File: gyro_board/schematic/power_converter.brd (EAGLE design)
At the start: 64 x 26 mm, 39 parts, among them M1 BSZ097N04LS_G

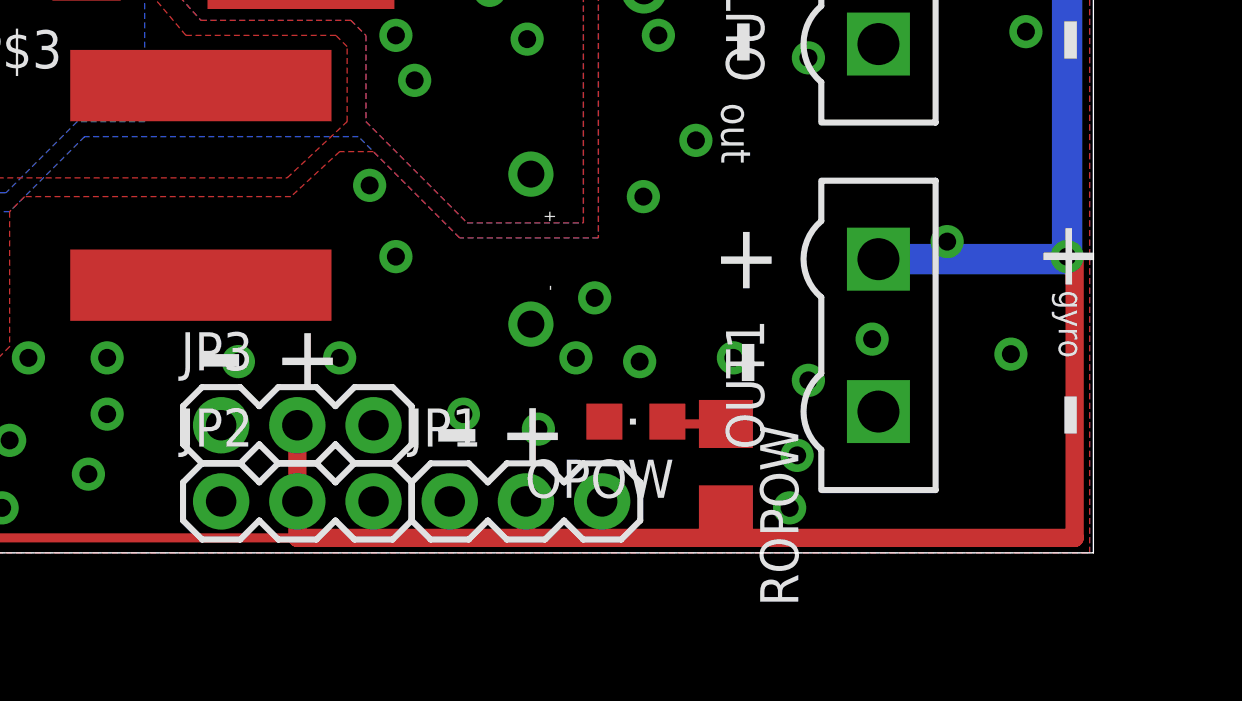
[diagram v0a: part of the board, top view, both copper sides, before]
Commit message: remembered to do a DRC and fixed the issues it found
git-svn-id: https://robotics.mvla.net/svn/frc971/2013/trunk/src@4030 f308d9b7-e957-4cde-b6ac-9a88185e7312
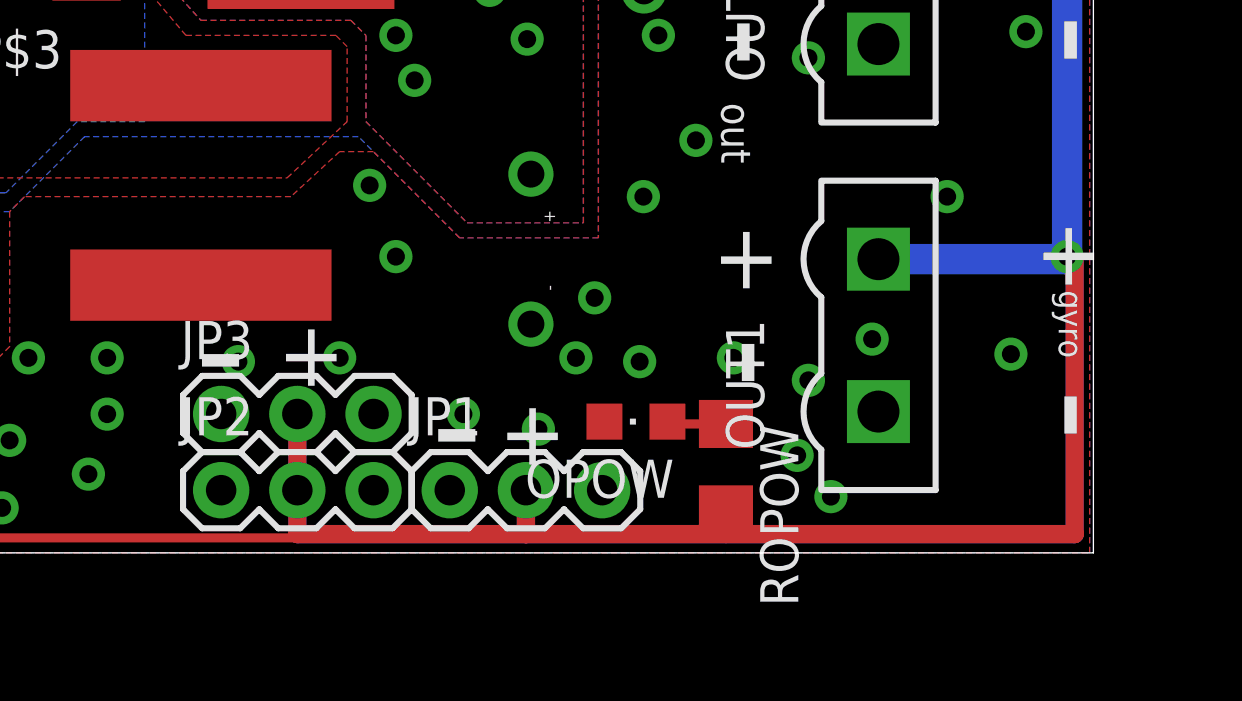
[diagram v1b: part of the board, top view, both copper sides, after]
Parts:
- moved JP1 0.38 mm to (42.5, 2.09)
- moved JP2 0.38 mm to (34.9, 2.09)
- moved JP3 0.38 mm to (34.9, 4.63)
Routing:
- net N$14: track 79.9 -> 121.1 mm
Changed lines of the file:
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@@
 <text x="60.861" y="5.444" size="3.81" layer="21" rot="R270">-</text>
 <text x="44.176" y="2.944" size="2.1844" layer="21">+</text>
-<text x="36.676" y="5.444" size="2.1844" layer="21">+</text>
+<text x="36.801" y="5.569" size="2.1844" layer="21">+</text>
 <text x="41.931" y="2.486" size="3.81" layer="21">-</text>
 <text x="34.056" y="4.986" size="3.81" layer="21">-</text>
@@
 </class>
 </classes>
-<designrules name="SparkFun *">
+<designrules name="SparkFun">
 <description language="en">&lt;b&gt;EAGLE Design Rules&lt;/b&gt;
 &lt;p&gt;
@@
 <param name="dpGapFactor" value="2.5"/>
 <param name="checkGrid" value="0"/>
-<param name="checkAngle" value="1"/>
+<param name="checkAngle" value="0"/>
 <param name="checkFont" value="1"/>
 <param name="checkRestrict" value="1"/>
@@
 <element name="COUT$1" library="custom_parts" package="RR71C331MDN1" value="" x="47.25" y="20.5" rot="R315"/>
 <element name="OUT1" library="custom_parts" package="ELFH0225*" value="POWER_CONNECTORELFH0225*" x="59.375" y="7.25" rot="R90"/>
-<element name="JP1" library="SparkFun-Connectors" package="1X03" value="" x="42.545" y="1.7145"/>
-<element name="JP2" library="SparkFun-Connectors" package="1X03" value="" x="34.925" y="1.7145"/>
-<element name="JP3" library="SparkFun-Connectors" package="1X03" value="" x="34.925" y="4.2545"/>
+<element name="JP1" library="SparkFun-Connectors" package="1X03" value="" x="42.545" y="2.0895"/>
+<element name="JP2" library="SparkFun-Connectors" package="1X03" value="" x="34.925" y="2.0895"/>
+<element name="JP3" library="SparkFun-Connectors" package="1X03" value="" x="34.925" y="4.6295"/>
 </elements>
 <signals>
@@
 <via x="54.5" y="5.75" extent="1-16" drill="0.6"/>
 <via x="54.125" y="3.25" extent="1-16" drill="0.6"/>
-<via x="53.875" y="1.5" extent="1-16" drill="0.6"/>
+<via x="55.25" y="1.875" extent="1-16" drill="0.6"/>
 <via x="48.875" y="6.375" extent="1-16" drill="0.6"/>
 <via x="43" y="4.625" extent="1-16" drill="0.6"/>
@@
 <via x="56.625" y="7.125" extent="1-16" drill="0.6"/>
 <via x="61.25" y="6.625" extent="1-16" drill="0.6"/>
-<via x="59.125" y="10.375" extent="1-16" drill="0.6"/>
+<via x="59.125" y="11.875" extent="1-16" drill="0.6"/>
 <via x="50.75" y="13.75" extent="1-16" drill="0.6"/>
 <via x="49.5" y="17.25" extent="1-16" drill="0.6"/>
@@
 <vertex x="63.875" y="20.875"/>
 </polygon>
-<wire x1="51.75" y1="1.453" x2="51.75" y2="0.5" width="0.3048" layer="1"/>
+<wire x1="51.75" y1="1.453" x2="51.75" y2="0.625" width="0.3048" layer="1"/>
 <via x="63.125" y="9.875" extent="1-16" drill="0.6"/>
-<wire x1="51.75" y1="0.5" x2="63.375" y2="0.5" width="0.6096" layer="1"/>
-<wire x1="63.375" y1="0.5" x2="63.375" y2="9.875" width="0.6096" layer="1"/>
+<wire x1="51.75" y1="0.625" x2="63.375" y2="0.625" width="0.6096" layer="1"/>
+<wire x1="63.375" y1="0.625" x2="63.375" y2="9.875" width="0.6096" layer="1"/>
 <wire x1="63.375" y1="9.875" x2="63.125" y2="9.875" width="0.3048" layer="1"/>
 <contactref element="OUT1" pad="P$1"/>
@@
 <contactref element="JP2" pad="2"/>
 <contactref element="JP3" pad="2"/>
-<wire x1="37.465" y1="4.2545" x2="37.465" y2="1.7145" width="0.6096" layer="1"/>
-<wire x1="37.465" y1="1.7145" x2="37.465" y2="0.5" width="0.6096" layer="1"/>
-<wire x1="37.465" y1="0.5" x2="45.085" y2="0.5" width="0.6096" layer="1"/>
-<wire x1="45.085" y1="0.5" x2="51.75" y2="0.5" width="0.6096" layer="1"/>
-<wire x1="45.085" y1="1.7145" x2="45.085" y2="0.5" width="0.6096" layer="1"/>
+<wire x1="37.465" y1="4.6295" x2="37.465" y2="2.0895" width="0.6096" layer="1"/>
+<wire x1="37.465" y1="2.0895" x2="37.465" y2="0.625" width="0.6096" layer="1"/>
+<wire x1="37.465" y1="0.625" x2="45.085" y2="0.625" width="0.6096" layer="1"/>
+<wire x1="45.085" y1="0.625" x2="51.75" y2="0.625" width="0.6096" layer="1"/>
+<wire x1="45.085" y1="2.0895" x2="45.085" y2="0.625" width="0.6096" layer="1"/>
 <wire x1="25.525" y1="2.125" x2="25.525" y2="0.5" width="0.3048" layer="1"/>
 <wire x1="25.525" y1="0.5" x2="37.465" y2="0.5" width="0.3048" layer="1"/>
+<wire x1="37.465" y1="0.5" x2="37.465" y2="0.625" width="0.3048" layer="1"/>
+<wire x1="63.375" y1="9.875" x2="63.375" y2="0.625" width="0.6096" layer="16"/>
+<wire x1="63.375" y1="0.625" x2="45.085" y2="0.625" width="0.6096" layer="16"/>
+<wire x1="45.085" y1="0.625" x2="37.465" y2="0.625" width="0.6096" layer="16"/>
+<wire x1="37.465" y1="0.625" x2="37.465" y2="4.625" width="0.6096" layer="16"/>
+<wire x1="45.085" y1="0.625" x2="45.085" y2="2.0895" width="0.6096" layer="16"/>
+<wire x1="63.375" y1="9.875" x2="63.125" y2="9.875" width="0.6096" layer="16"/>
 </signal>
 <signal name="N$2">

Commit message: moved the connectors away from the edge
git-svn-id: https://robotics.mvla.net/svn/frc971/2013/trunk/src@4031 f308d9b7-e957-4cde-b6ac-9a88185e7312
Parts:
- moved IN 0.38 mm to (4.38, 18.1)
- moved OUT 0.38 mm to (59.8, 19.5)
- moved OUT1 0.38 mm to (59.8, 7.25)
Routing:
- net N$14: track 121.1 -> 120.4 mm
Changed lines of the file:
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@@
 <text x="62.051" y="8.944" size="2.1844" layer="21">+</text>
 <text x="62.051" y="22.194" size="2.1844" layer="21">+</text>
-<text x="0.176" y="18.694" size="2.1844" layer="21">+</text>
-<text x="0.73" y="17.354" size="1" layer="21" font="vector" ratio="10" rot="SR270">in</text>
-<text x="2.763" y="13.431" size="3.81" layer="21" rot="R90">-</text>
+<text x="-0.074" y="18.694" size="2.1844" layer="21">+</text>
+<text x="0.48" y="17.354" size="1" layer="21" font="vector" ratio="10" rot="SR270">in</text>
+<text x="2.263" y="13.431" size="3.81" layer="21" rot="R90">-</text>
 <text x="60.861" y="17.944" size="3.81" layer="21" rot="R270">-</text>
 <text x="60.861" y="5.444" size="3.81" layer="21" rot="R270">-</text>
@@
 <element name="CIN$1" library="resistor" package="C1210" value="C3225X7R1E106M" x="3.25" y="3.5"/>
 <element name="CIN$2" library="resistor" package="C1210" value="C3225X7R1E106M" x="3.25" y="6.75"/>
-<element name="IN" library="custom_parts" package="ELFH0225*" value="POWER_CONNECTORELFH0225*" x="4.75" y="18.125" rot="R270"/>
-<element name="OUT" library="custom_parts" package="ELFH0225*" value="POWER_CONNECTORELFH0225*" x="59.375" y="19.5" rot="R90"/>
+<element name="IN" library="custom_parts" package="ELFH0225*" value="POWER_CONNECTORELFH0225*" x="4.375" y="18.125" rot="R270"/>
+<element name="OUT" library="custom_parts" package="ELFH0225*" value="POWER_CONNECTORELFH0225*" x="59.75" y="19.5" rot="R90"/>
 <element name="DTVS" library="custom_parts" package="SOD-123" value="MMSZ5246BT1G" x="3.25" y="1" rot="R180"/>
 <element name="IPOW" library="led" package="CHIPLED_0805" value="" x="11" y="5.75" rot="R90"/>
@@
 <element name="COUT$0" library="custom_parts" package="RR71C331MDN1" value="" x="45.25" y="10.125" rot="R270"/>
 <element name="COUT$1" library="custom_parts" package="RR71C331MDN1" value="" x="47.25" y="20.5" rot="R315"/>
-<element name="OUT1" library="custom_parts" package="ELFH0225*" value="POWER_CONNECTORELFH0225*" x="59.375" y="7.25" rot="R90"/>
+<element name="OUT1" library="custom_parts" package="ELFH0225*" value="POWER_CONNECTORELFH0225*" x="59.75" y="7.25" rot="R90"/>
 <element name="JP1" library="SparkFun-Connectors" package="1X03" value="" x="42.545" y="2.0895"/>
 <element name="JP2" library="SparkFun-Connectors" package="1X03" value="" x="34.925" y="2.0895"/>
@@
 <wire x1="63.125" y1="9.79" x2="63.125" y2="9.875" width="1.016" layer="16"/>
 <wire x1="63.125" y1="9.875" x2="63.125" y2="22.04" width="1.016" layer="16"/>
-<wire x1="63.125" y1="22.04" x2="56.835" y2="22.04" width="1.016" layer="16"/>
+<wire x1="63.125" y1="22.04" x2="57.21" y2="22.04" width="1.016" layer="16"/>
 <via x="54.625" y="23.375" extent="1-16" drill="0.6"/>
 <via x="51.875" y="23.5" extent="1-16" drill="0.6"/>
@@
 <wire x1="63.375" y1="9.875" x2="63.125" y2="9.875" width="0.3048" layer="1"/>
 <contactref element="OUT1" pad="P$1"/>
-<wire x1="63.125" y1="9.79" x2="56.835" y2="9.79" width="1.016" layer="16"/>
+<wire x1="63.125" y1="9.79" x2="57.21" y2="9.79" width="1.016" layer="16"/>
 <contactref element="JP1" pad="2"/>
 <contactref element="JP2" pad="2"/>
